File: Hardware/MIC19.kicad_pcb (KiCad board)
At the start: 2 copper layers, 160 x 70 mm, 101 parts, among them J101 SW_BOAT_ON, J102 ENGINE_VEL, J103 SW_PUMP1_ON, J104 SW_ENGINE_ON, J105 ENGINE_ACEL, J106 SW_PUMP2_ON, J107 SW_MPPT_ON, J108 MPPT_POT, J109 SW_PUMP3_ON, J110 SW_DMS, J111 SW_EMERGENCIA, J401 USART, J402 BUZZER ON/OFF, J601 RJ45, J602 RJ45, Q101 BCV27, U201 MCP2551-I/SN, U202 MCP2515-xSO, U401 ATMEGA328P-PU, U501 LM7805, Y201 16MHz, Y401 16MHz

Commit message: Modelo final
Terminado os conectores e a topologia
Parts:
- removed J402: BUZZER ON/OFF, Connector_PinHeader_2.54mm:PinHeader_1x02_P2.54mm_Vertical
- moved R115 9.53 mm to (75.5, 74.7), turned to 270 degrees
- moved R109 9.30 mm to (94.5, 74.7), turned to 270 degrees
- moved C103 9.01 mm to (103.5, 74.7), turned to 270 degrees
- moved R103 7.81 mm to (113.5, 74.7), turned to 270 degrees
- moved TP203 7.46 mm to (162.7, 129.4)
- moved R102 7.42 mm to (170.3, 74.7), turned to 270 degrees
- moved C108 6.78 mm to (122.5, 74.7), turned to 270 degrees
- moved C109 6.47 mm to (65.5, 74.7), turned to 270 degrees
- moved C106 6.30 mm to (84.5, 74.7), turned to 270 degrees
- moved R108 6.11 mm to (151.5, 74.7), turned to 270 degrees
- moved C105 5.57 mm to (141.5, 74.7), turned to 270 degrees
- moved R114 5.53 mm to (132.5, 74.7), turned to 270 degrees
- moved C102 5.38 mm to (160.3, 74.7), turned to 270 degrees
- moved R112 3.82 mm to (89.5, 74.7), turned to 90 degrees
- moved R105 2.19 mm to (165.3, 74.7), turned to 90 degrees
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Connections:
- D403 pad 1: Net-(D403-Pad1) -> Net-(BZ1-Pad1)
- Q101 pad 3: Net-(D403-Pad1) -> Net-(BZ1-Pad1)
- RV401 pad 1: Net-(D403-Pad1) -> Net-(BZ1-Pad1)
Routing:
- net +5V: track 143.4 -> 576.4 mm, vias 4 -> 26
- net /Conectores/ENGINE_VEL: track 0.00 -> 80.5 mm
- net /Conectores/ENGINE_ACEL: track 0.00 -> 63.4 mm
- net Net-(D403-Pad1): track 54.6 -> 0.00 mm
- net Net-(BZ1-Pad1): track 10.1 -> 64.6 mm
- net /Conectores/MPPT_POT: track 0.00 -> 47.0 mm
- net GND: track 90.7 -> 136.9 mm, vias 11 -> 17
- net /Conectores/SW_PUMP3_ON: track 0.00 -> 44.2 mm
- net /CANBUS/CS: track 21.9 -> 56.5 mm
- net /MISO: track 32.8 -> 66.0 mm
- net /MOSI: track 27.9 -> 60.2 mm
- net /Conectores/SW_PUMP1_ON: track 0.00 -> 32.2 mm
- net /Conectores/SW_PUMP2_ON: track 0.00 -> 31.5 mm
- net /SCK: track 30.8 -> 51.3 mm
- net /CANBUS/INT: track 16.8 -> 36.8 mm
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- added copper zone on B.Cu, net GND

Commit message: Buzzer estava invertido, alimentações melhoradas. A alimentação do atmega foi isolada em relação aos switches.
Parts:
- moved R406 13.0 mm to (59.8, 102.5)
- moved D403 8.16 mm to (59.8, 107.0), turned to 90 degrees
- moved C407 7.00 mm to (68.4, 108.1)
- moved Q101 7.00 mm to (63.9, 108.1)
- moved R404 7.00 mm to (73.4, 108.1)
- moved R405 7.00 mm to (70.9, 108.1)
- moved RV401 6.73 mm to (63.0, 99.0)
- moved D402 6.30 mm to (69.2, 99.8), turned to 270 degrees
- moved BZ1 6.25 mm to (72.5, 96.3)
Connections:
- D402 pad 1: Net-(BZ1-Pad2) -> Net-(BZ1-Pad1)
- D402 pad 2: Net-(BZ1-Pad1) -> Net-(BZ1-Pad2)
- D403 pad 1: Net-(BZ1-Pad1) -> Net-(BZ1-Pad2)
- Q101 pad 3: Net-(BZ1-Pad1) -> Net-(BZ1-Pad2)
- RV401 pad 1: Net-(BZ1-Pad1) -> +5V
- RV401 pad 2: Net-(BZ1-Pad2) -> Net-(BZ1-Pad1)
- RV401 pad 3: +5V -> Net-(BZ1-Pad2)
- U201 pad 5: Net-(U201-Pad5) -> (no net)
- U202 pad 10: Net-(U202-Pad10) -> (no net)
- U202 pad 11: Net-(U202-Pad11) -> (no net)
- U202 pad 3: Net-(U202-Pad3) -> (no net)
- U202 pad 4: Net-(U202-Pad4) -> (no net)
- U202 pad 5: Net-(U202-Pad5) -> (no net)
- U202 pad 6: Net-(U202-Pad6) -> (no net)
- U401 pad 16: Net-(U401-Pad16) -> (no net)
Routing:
- net Net-(BZ1-Pad1): track 64.6 -> 12.8 mm
- net +5V: track 576.4 -> 561.0 mm, vias 26 -> 24
- net /MCU/BUZZER: track 47.8 -> 40.7 mm
- net GND: track 136.9 -> 129.9 mm, vias 17 -> 15
- net Net-(BZ1-Pad2): track 16.5 -> 17.7 mm
- net /Conectores/MPPT_POT: track 47.0 -> 47.6 mm
- net /CANBUS CONN/CAN_H: track 63.3 -> 62.8 mm

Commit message: Roteamento de alimentação alterado e placa compactada.
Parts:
- moved C205 20.6 mm to (153.5, 119.2), turned to 90 degrees
- moved C204 13.7 mm to (135.7, 124.0)
- moved R203 13.7 mm to (147.3, 107.5)
- moved TP201 13.7 mm to (141.0, 103.6)
- moved TP202 13.7 mm to (144.2, 103.6)
- moved TP205 13.7 mm to (147.3, 103.6)
- moved TP206 13.7 mm to (137.8, 103.6)
- moved U202 13.7 mm to (142.0, 115.8)
- moved Y201 13.7 mm to (142.0, 126.6)
- moved C203 13.7 mm to (139.5, 126.2)
- moved D501 13.6 mm to (170.2, 88.8)
- moved TP204 13.5 mm to (150.8, 122.0)
- moved F501 13.3 mm to (167.2, 90.0)
- moved C501 12.4 mm to (163.8, 90.8)
- moved TP203 12.0 mm to (150.8, 128.5)
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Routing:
- net +5V: track 561.0 -> 630.6 mm, vias 24 -> 26
- net GND: track 129.9 -> 177.4 mm, vias 15 -> 12
- net /CANBUS/CS: track 56.5 -> 39.0 mm
- net /MISO: track 66.0 -> 49.2 mm
- net /MOSI: track 60.2 -> 44.9 mm
- net /CANBUS/INT: track 36.8 -> 25.8 mm
- net /CANBUS/TXCAN: track 14.1 -> 23.9 mm
- net /SCK: track 51.3 -> 42.0 mm
- net /POWER SUPPLY/+18V_IN: track 57.5 -> 65.1 mm
- net /CANBUS/RXCAN: track 16.7 -> 23.8 mm
- net /CANBUS CONN/CAN_H: track 62.8 -> 58.4 mm
- net Net-(R202-Pad1): track 6.64 -> 2.83 mm
- net Net-(C501-Pad1): track 19.5 -> 15.8 mm
- net Net-(J401-Pad2): track 6.59 -> 3.46 mm
- net Net-(J401-Pad3): track 6.59 -> 3.46 mm
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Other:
- board size 160 x 70 mm -> 160 x 70.2 mm

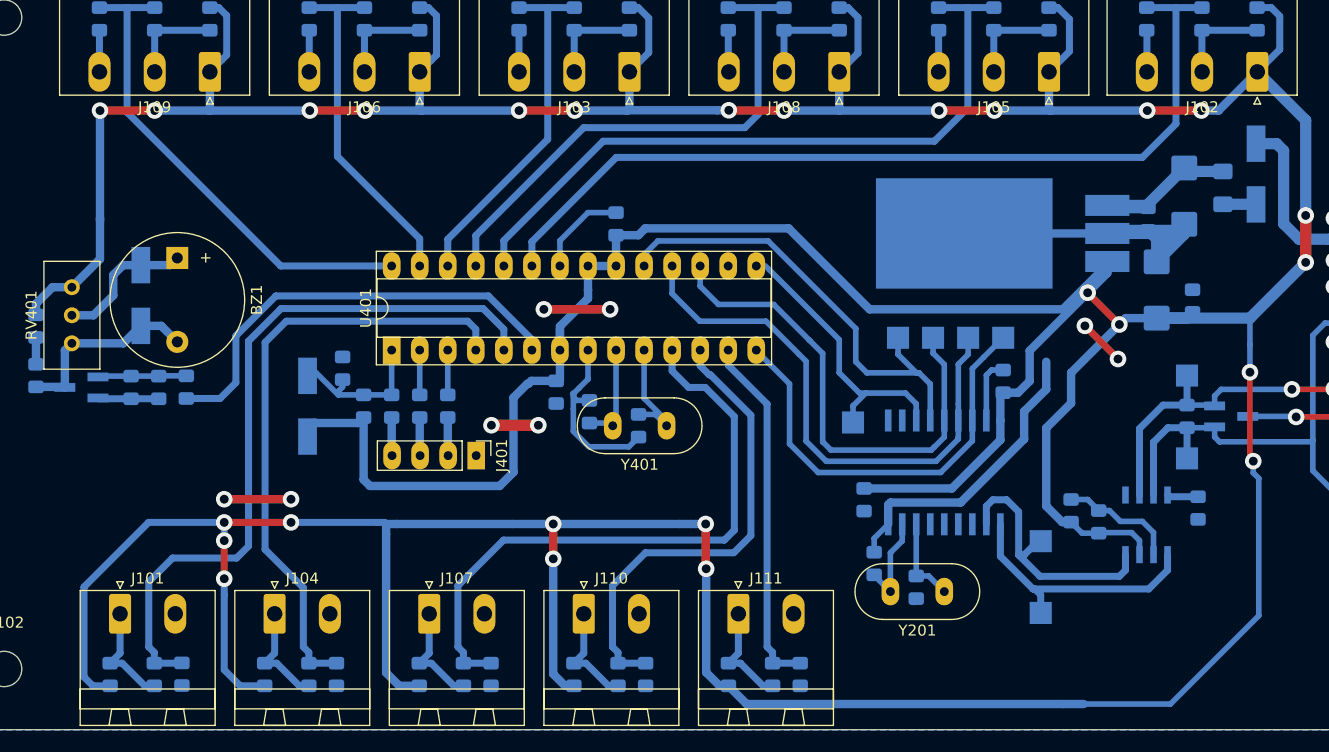
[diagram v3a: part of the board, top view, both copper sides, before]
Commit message: Final
Terminado detalhes que eram necessário para finalizar a placa, como trilhas de Vcc e Gnd remodeladas para melhor fluxo da corrente
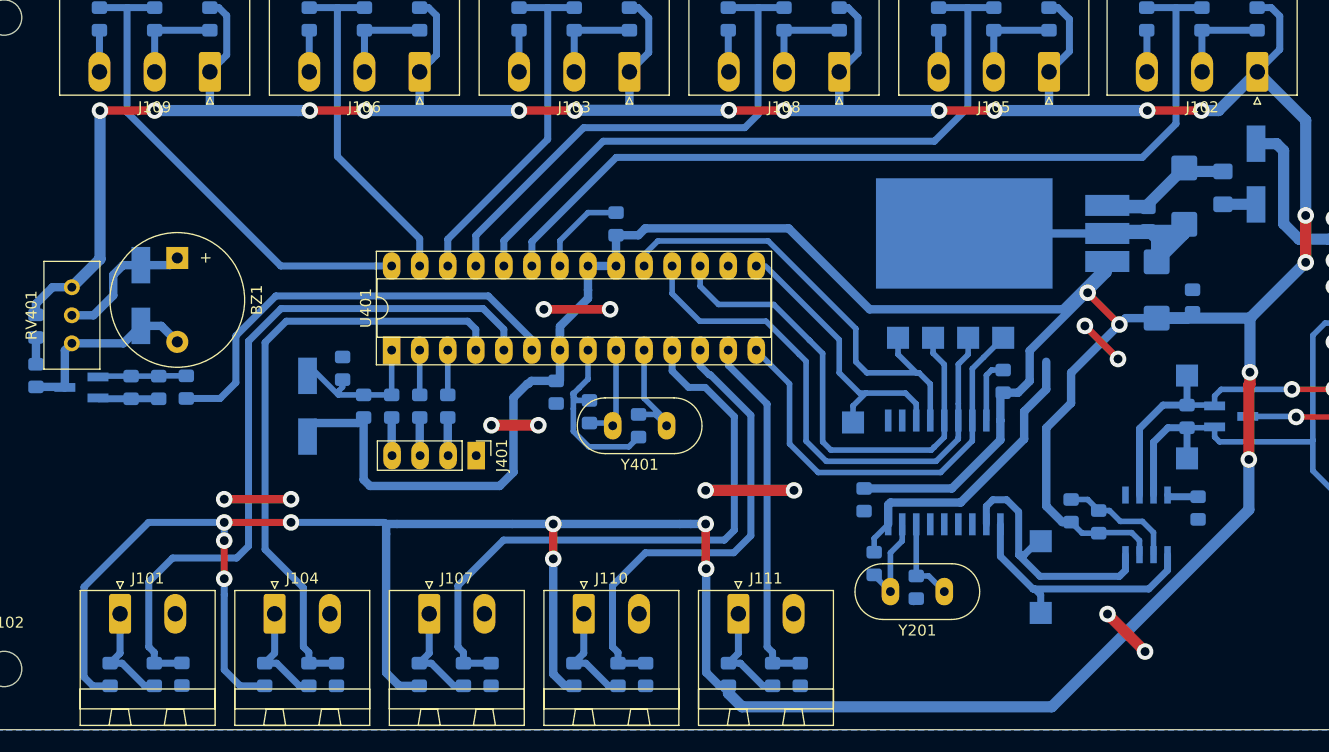
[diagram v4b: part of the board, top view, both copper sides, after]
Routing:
- net GND: track 177.4 -> 190.2 mm, vias 12 -> 16
- net +5V: track 630.6 -> 623.3 mm
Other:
- net class Default: clearance 0.508 -> 0.3
- net class power: clearance 0.762 -> 0.3
- rule trace_clearance: 0.508 -> 0.3

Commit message: Conferido e Finalizado
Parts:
- removed C405: 100nF, Capacitor_SMD:C_0805_2012Metric_Pad1.15x1.40mm_HandSolder
- added BZ1: Buzzer, Buzzer_Beeper:Buzzer_12x9.5RM7.6, F.Cu at (221.3, 158.4)
- added BZ1: Buzzer, Buzzer_Beeper:Buzzer_12x9.5RM7.6, F.Cu at (56.5, 136.3)
- added C101: 100n, Capacitor_SMD:C_0805_2012Metric_Pad1.15x1.40mm_HandSolder, B.Cu at (259.1, 158.0)
- added C101: 100n, Capacitor_SMD:C_0805_2012Metric_Pad1.15x1.40mm_HandSolder, B.Cu at (57.0, 174.1)
- added C102: 100n, Capacitor_SMD:C_0805_2012Metric_Pad1.15x1.40mm_HandSolder, B.Cu at (199.7, 70.7)
- added C102: 100n, Capacitor_SMD:C_0805_2012Metric_Pad1.15x1.40mm_HandSolder, B.Cu at (144.3, 114.7)
- added C103: 100n, Capacitor_SMD:C_0805_2012Metric_Pad1.15x1.40mm_HandSolder, B.Cu at (199.7, 127.5)
- added C103: 100n, Capacitor_SMD:C_0805_2012Metric_Pad1.15x1.40mm_HandSolder, B.Cu at (87.5, 114.7)
- added C104: 100n, Capacitor_SMD:C_0805_2012Metric_Pad1.15x1.40mm_HandSolder, B.Cu at (259.1, 144.0)
- added C104: 100n, Capacitor_SMD:C_0805_2012Metric_Pad1.15x1.40mm_HandSolder, B.Cu at (71.0, 174.1)
- added C105: 100n, Capacitor_SMD:C_0805_2012Metric_Pad1.15x1.40mm_HandSolder, B.Cu at (199.7, 89.5)
- added C105: 100n, Capacitor_SMD:C_0805_2012Metric_Pad1.15x1.40mm_HandSolder, B.Cu at (125.5, 114.7)
- added C106: 100n, Capacitor_SMD:C_0805_2012Metric_Pad1.15x1.40mm_HandSolder, B.Cu at (199.7, 146.5)
- added C106: 100n, Capacitor_SMD:C_0805_2012Metric_Pad1.15x1.40mm_HandSolder, B.Cu at (68.5, 114.7)
- added C107: 100n, Capacitor_SMD:C_0805_2012Metric_Pad1.15x1.40mm_HandSolder, B.Cu at (259.1, 130.0)
- added C107: 100n, Capacitor_SMD:C_0805_2012Metric_Pad1.15x1.40mm_HandSolder, B.Cu at (85.0, 174.1)
- added C108: 100n, Capacitor_SMD:C_0805_2012Metric_Pad1.15x1.40mm_HandSolder, B.Cu at (199.7, 108.5)
- added C108: 100n, Capacitor_SMD:C_0805_2012Metric_Pad1.15x1.40mm_HandSolder, B.Cu at (106.5, 114.7)
- added C109: 100n, Capacitor_SMD:C_0805_2012Metric_Pad1.15x1.40mm_HandSolder, B.Cu at (199.7, 165.5)
- added C109: 100n, Capacitor_SMD:C_0805_2012Metric_Pad1.15x1.40mm_HandSolder, B.Cu at (49.5, 114.7)
- added C110: 100n, Capacitor_SMD:C_0805_2012Metric_Pad1.15x1.40mm_HandSolder, B.Cu at (259.1, 116.0)
- added C110: 100n, Capacitor_SMD:C_0805_2012Metric_Pad1.15x1.40mm_HandSolder, B.Cu at (99.0, 174.1)
- added C111: 100n, Capacitor_SMD:C_0805_2012Metric_Pad1.15x1.40mm_HandSolder, B.Cu at (258.1, 96.8)
- added C111: 100n, Capacitor_SMD:C_0805_2012Metric_Pad1.15x1.40mm_HandSolder, B.Cu at (118.2, 173.1)
- added C201: 100nF, Capacitor_SMD:C_0805_2012Metric_Pad1.15x1.40mm_HandSolder, B.Cu at (243.2, 96.2)
- added C201: 100nF, Capacitor_SMD:C_0805_2012Metric_Pad1.15x1.40mm_HandSolder, B.Cu at (118.8, 158.2)
- added C202: 100nF, Capacitor_SMD:C_0805_2012Metric_Pad1.15x1.40mm_HandSolder, B.Cu at (245.2, 75.0)
- added C202: 100nF, Capacitor_SMD:C_0805_2012Metric_Pad1.15x1.40mm_HandSolder, B.Cu at (140.0, 160.2)
- added C203: 22pF, Capacitor_SMD:C_0805_2012Metric_Pad1.15x1.40mm_HandSolder, B.Cu at (251.2, 91.5)
- added C203: 22pF, Capacitor_SMD:C_0805_2012Metric_Pad1.15x1.40mm_HandSolder, B.Cu at (123.5, 166.2)
- added C204: 22pF, Capacitor_SMD:C_0805_2012Metric_Pad1.15x1.40mm_HandSolder, B.Cu at (249.0, 95.3)
- added C204: 22pF, Capacitor_SMD:C_0805_2012Metric_Pad1.15x1.40mm_HandSolder, B.Cu at (119.7, 164.0)
- added C205: 100nF, Capacitor_SMD:C_0805_2012Metric_Pad1.15x1.40mm_HandSolder, B.Cu at (244.2, 77.5)
- added C205: 100nF, Capacitor_SMD:C_0805_2012Metric_Pad1.15x1.40mm_HandSolder, B.Cu at (137.5, 159.2)
- added C401: 100nF, Capacitor_SMD:C_0805_2012Metric_Pad1.15x1.40mm_HandSolder, B.Cu at (218.3, 118.7)
- added C401: 100nF, Capacitor_SMD:C_0805_2012Metric_Pad1.15x1.40mm_HandSolder, B.Cu at (96.3, 133.3)
- added C402: 100nF, Capacitor_SMD:C_0805_2012Metric_Pad1.15x1.40mm_HandSolder, B.Cu at (233.5, 124.1)
- added C402: 100nF, Capacitor_SMD:C_0805_2012Metric_Pad1.15x1.40mm_HandSolder, B.Cu at (90.9, 148.5)
- added C403: 22pF, Capacitor_SMD:C_0805_2012Metric_Pad1.15x1.40mm_HandSolder, B.Cu at (236.5, 116.7)
- added C403: 22pF, Capacitor_SMD:C_0805_2012Metric_Pad1.15x1.40mm_HandSolder, B.Cu at (98.3, 151.5)
- added C404: 22pF, Capacitor_SMD:C_0805_2012Metric_Pad1.15x1.40mm_HandSolder, B.Cu at (235.3, 121.1)
- added C404: 22pF, Capacitor_SMD:C_0805_2012Metric_Pad1.15x1.40mm_HandSolder, B.Cu at (93.9, 150.3)
- added C406: 10nF, Capacitor_SMD:C_0805_2012Metric_Pad1.15x1.40mm_HandSolder, B.Cu at (231.3, 143.5)
- added C406: 10nF, Capacitor_SMD:C_0805_2012Metric_Pad1.15x1.40mm_HandSolder, B.Cu at (71.5, 146.3)
- added C407: 100nF, Capacitor_SMD:C_0805_2012Metric_Pad1.15x1.40mm_HandSolder, B.Cu at (233.1, 162.6)
- added C407: 100nF, Capacitor_SMD:C_0805_2012Metric_Pad1.15x1.40mm_HandSolder, B.Cu at (52.4, 148.1)
- added C501: 1uF, Capacitor_Tantalum_SMD:CP_EIA-6032-20_AVX-F_Pad2.25x2.35mm_HandSolder, B.Cu at (215.8, 67.2)
- added C501: 1uF, Capacitor_Tantalum_SMD:CP_EIA-6032-20_AVX-F_Pad2.25x2.35mm_HandSolder, B.Cu at (147.8, 130.8)
- added C502: 100nF, Capacitor_SMD:C_0805_2012Metric_Pad1.15x1.40mm_HandSolder, B.Cu at (217.8, 70.5)
- added C502: 100nF, Capacitor_SMD:C_0805_2012Metric_Pad1.15x1.40mm_HandSolder, B.Cu at (144.5, 132.8)
- added C503: 100nF, Capacitor_SMD:C_0805_2012Metric_Pad1.15x1.40mm_HandSolder, B.Cu at (225.2, 66.5)
- added C503: 100nF, Capacitor_SMD:C_0805_2012Metric_Pad1.15x1.40mm_HandSolder, B.Cu at (148.5, 140.2)
- added C504: 1uF, Capacitor_Tantalum_SMD:CP_EIA-6032-20_AVX-F_Pad2.25x2.35mm_HandSolder, B.Cu at (224.2, 69.8)
- added C504: 1uF, Capacitor_Tantalum_SMD:CP_EIA-6032-20_AVX-F_Pad2.25x2.35mm_HandSolder, B.Cu at (145.2, 139.2)
- added D201: pesd1can, Package_TO_SOT_SMD:SOT-23_Handsoldering, B.Cu at (235.7, 63.0)
- added D201: pesd1can, Package_TO_SOT_SMD:SOT-23_Handsoldering, B.Cu at (152.0, 150.7)
- added D401: LL4148, Diode_SMD:D_MiniMELF_Handsoldering, B.Cu at (234.8, 146.7)
- added D401: LL4148, Diode_SMD:D_MiniMELF_Handsoldering, B.Cu at (68.3, 149.8)
- added D402: BYD77, Diode_SMD:D_MiniMELF_Handsoldering, B.Cu at (224.8, 161.8)
- added D402: BYD77, Diode_SMD:D_MiniMELF_Handsoldering, B.Cu at (53.2, 139.8)
- added D403: LED_RED, LED_SMD:LED_0805_2012Metric_Pad1.15x1.40mm_HandSolder, B.Cu at (232.0, 171.2)
- added D403: LED_RED, LED_SMD:LED_0805_2012Metric_Pad1.15x1.40mm_HandSolder, B.Cu at (43.8, 147.0)
- added D501: LL4148, Diode_SMD:D_MiniMELF_Handsoldering, B.Cu at (213.8, 60.8)
- added D501: LL4148, Diode_SMD:D_MiniMELF_Handsoldering, B.Cu at (154.2, 128.8)
- added F501: 500mA, Fuse:Fuse_1206_3216Metric_Pad1.42x1.75mm_HandSolder, B.Cu at (215.0, 63.8)
- added F501: 500mA, Fuse:Fuse_1206_3216Metric_Pad1.42x1.75mm_HandSolder, B.Cu at (151.2, 130.0)
- added H101: MountingHole, MountingHole:MountingHole_3.2mm_M3, F.Cu at (199.6, 174.1)
- added H101: MountingHole, MountingHole:MountingHole_3.2mm_M3, F.Cu at (40.9, 114.6)
- added H102: MountingHole, MountingHole:MountingHole_3.2mm_M3, F.Cu at (258.6, 174.1)
- added H102: MountingHole, MountingHole:MountingHole_3.2mm_M3, F.Cu at (40.9, 173.6)
- added H103: MountingHole, MountingHole:MountingHole_3.2mm_M3, F.Cu at (199.3, 35.1)
- added H103: MountingHole, MountingHole:MountingHole_3.2mm_M3, F.Cu at (179.9, 114.3)
- added H104: MountingHole, MountingHole:MountingHole_3.2mm_M3, F.Cu at (258.3, 34.6)
- added H104: MountingHole, MountingHole:MountingHole_3.2mm_M3, F.Cu at (180.4, 173.3)
- added J101: SW_BOAT_ON, Connector_Phoenix_MSTB:PhoenixContact_MSTBA_2,5_2-G_1x02_P5.00mm_Horizontal, F.Cu at (253.6, 163.6)
- added J101: SW_BOAT_ON, Connector_Phoenix_MSTB:PhoenixContact_MSTBA_2,5_2-G_1x02_P5.00mm_Horizontal, F.Cu at (51.4, 168.6)
- added J102: ENGINE_VEL, Connector_Phoenix_MSTB:PhoenixContact_MSTBA_2,5_3-G_1x03_P5.00mm_Horizontal, F.Cu at (204.5, 60.6)
- added J102: ENGINE_VEL, Connector_Phoenix_MSTB:PhoenixContact_MSTBA_2,5_3-G_1x03_P5.00mm_Horizontal, F.Cu at (154.4, 119.5)
- added J103: SW_PUMP1_ON, Connector_Phoenix_MSTB:PhoenixContact_MSTBA_2,5_3-G_1x03_P5.00mm_Horizontal, F.Cu at (204.5, 117.5)
- added J103: SW_PUMP1_ON, Connector_Phoenix_MSTB:PhoenixContact_MSTBA_2,5_3-G_1x03_P5.00mm_Horizontal, F.Cu at (97.5, 119.5)
- added J104: SW_ENGINE_ON, Connector_Phoenix_MSTB:PhoenixContact_MSTBA_2,5_2-G_1x02_P5.00mm_Horizontal, F.Cu at (253.6, 149.6)
- added J104: SW_ENGINE_ON, Connector_Phoenix_MSTB:PhoenixContact_MSTBA_2,5_2-G_1x02_P5.00mm_Horizontal, F.Cu at (65.4, 168.6)
- added J105: ENGINE_ACEL, Connector_Phoenix_MSTB:PhoenixContact_MSTBA_2,5_3-G_1x03_P5.00mm_Horizontal, F.Cu at (204.5, 79.5)
- added J105: ENGINE_ACEL, Connector_Phoenix_MSTB:PhoenixContact_MSTBA_2,5_3-G_1x03_P5.00mm_Horizontal, F.Cu at (135.5, 119.5)
- added J106: SW_PUMP2_ON, Connector_Phoenix_MSTB:PhoenixContact_MSTBA_2,5_3-G_1x03_P5.00mm_Horizontal, F.Cu at (204.5, 136.5)
- added J106: SW_PUMP2_ON, Connector_Phoenix_MSTB:PhoenixContact_MSTBA_2,5_3-G_1x03_P5.00mm_Horizontal, F.Cu at (78.5, 119.5)
- added J107: SW_MPPT_ON, Connector_Phoenix_MSTB:PhoenixContact_MSTBA_2,5_2-G_1x02_P5.00mm_Horizontal, F.Cu at (253.6, 135.6)
- added J107: SW_MPPT_ON, Connector_Phoenix_MSTB:PhoenixContact_MSTBA_2,5_2-G_1x02_P5.00mm_Horizontal, F.Cu at (79.4, 168.6)
- added J108: MPPT_POT, Connector_Phoenix_MSTB:PhoenixContact_MSTBA_2,5_3-G_1x03_P5.00mm_Horizontal, F.Cu at (204.5, 98.5)
- added J108: MPPT_POT, Connector_Phoenix_MSTB:PhoenixContact_MSTBA_2,5_3-G_1x03_P5.00mm_Horizontal, F.Cu at (116.5, 119.5)
- added J109: SW_PUMP3_ON, Connector_Phoenix_MSTB:PhoenixContact_MSTBA_2,5_3-G_1x03_P5.00mm_Horizontal, F.Cu at (204.5, 155.5)
- added J109: SW_PUMP3_ON, Connector_Phoenix_MSTB:PhoenixContact_MSTBA_2,5_3-G_1x03_P5.00mm_Horizontal, F.Cu at (59.5, 119.5)
- added J110: SW_DMS, Connector_Phoenix_MSTB:PhoenixContact_MSTBA_2,5_2-G_1x02_P5.00mm_Horizontal, F.Cu at (253.6, 121.6)
- added J110: SW_DMS, Connector_Phoenix_MSTB:PhoenixContact_MSTBA_2,5_2-G_1x02_P5.00mm_Horizontal, F.Cu at (93.4, 168.6)
- added J111: SW_EMERGENCIA, Connector_Phoenix_MSTB:PhoenixContact_MSTBA_2,5_2-G_1x02_P5.00mm_Horizontal, F.Cu at (253.6, 107.6)
- added J111: SW_EMERGENCIA, Connector_Phoenix_MSTB:PhoenixContact_MSTBA_2,5_2-G_1x02_P5.00mm_Horizontal, F.Cu at (107.4, 168.6)
- added J401: USART, Connector_PinHeader_2.54mm:PinHeader_1x04_P2.54mm_Vertical, F.Cu at (239.2, 131.4)
- added J401: USART, Connector_PinHeader_2.54mm:PinHeader_1x04_P2.54mm_Vertical, F.Cu at (83.6, 154.2)
- added J601: RJ45, KicadZeniteSolarLibrary18:RJ45_YH59_01, F.Cu at (223.5, 46.7)
- added J601: RJ45, KicadZeniteSolarLibrary18:RJ45_YH59_01, F.Cu at (168.3, 138.5)
- added J602: RJ45, KicadZeniteSolarLibrary18:RJ45_YH59_01, F.Cu at (244.3, 46.7)
- added J602: RJ45, KicadZeniteSolarLibrary18:RJ45_YH59_01, F.Cu at (168.3, 159.3)
- added Q101: BCV27, Package_TO_SOT_SMD:SOT-23_Handsoldering, B.Cu at (233.1, 167.1)
- added Q101: BCV27, Package_TO_SOT_SMD:SOT-23_Handsoldering, B.Cu at (47.9, 148.1)
- added R101: 10k, Resistor_SMD:R_0805_2012Metric_Pad1.15x1.40mm_HandSolder, B.Cu at (259.1, 164.5)
- added R101: 10k, Resistor_SMD:R_0805_2012Metric_Pad1.15x1.40mm_HandSolder, B.Cu at (50.5, 174.1)
- added R102: 10k, Resistor_SMD:R_0805_2012Metric_Pad1.15x1.40mm_HandSolder, B.Cu at (199.7, 60.6)
- added R102: 10k, Resistor_SMD:R_0805_2012Metric_Pad1.15x1.40mm_HandSolder, B.Cu at (154.3, 114.7)
- added R103: 10k, Resistor_SMD:R_0805_2012Metric_Pad1.15x1.40mm_HandSolder, B.Cu at (199.7, 117.5)
- added R103: 10k, Resistor_SMD:R_0805_2012Metric_Pad1.15x1.40mm_HandSolder, B.Cu at (97.5, 114.7)
- added R104: 100R, Resistor_SMD:R_0805_2012Metric_Pad1.15x1.40mm_HandSolder, B.Cu at (259.1, 160.5)
- added R104: 100R, Resistor_SMD:R_0805_2012Metric_Pad1.15x1.40mm_HandSolder, B.Cu at (54.5, 174.1)
- added R105: 100R, Resistor_SMD:R_0805_2012Metric_Pad1.15x1.40mm_HandSolder, B.Cu at (199.7, 65.7)
- added R105: 100R, Resistor_SMD:R_0805_2012Metric_Pad1.15x1.40mm_HandSolder, B.Cu at (149.3, 114.7)
- added R106: 100R, Resistor_SMD:R_0805_2012Metric_Pad1.15x1.40mm_HandSolder, B.Cu at (199.7, 122.5)
- added R106: 100R, Resistor_SMD:R_0805_2012Metric_Pad1.15x1.40mm_HandSolder, B.Cu at (92.5, 114.7)
- added R107: 10k, Resistor_SMD:R_0805_2012Metric_Pad1.15x1.40mm_HandSolder, B.Cu at (259.1, 150.5)
- added R107: 10k, Resistor_SMD:R_0805_2012Metric_Pad1.15x1.40mm_HandSolder, B.Cu at (64.5, 174.1)
- added R108: 10k, Resistor_SMD:R_0805_2012Metric_Pad1.15x1.40mm_HandSolder, B.Cu at (199.7, 79.5)
- added R108: 10k, Resistor_SMD:R_0805_2012Metric_Pad1.15x1.40mm_HandSolder, B.Cu at (135.5, 114.7)
- added R109: 10k, Resistor_SMD:R_0805_2012Metric_Pad1.15x1.40mm_HandSolder, B.Cu at (199.7, 136.5)
- added R109: 10k, Resistor_SMD:R_0805_2012Metric_Pad1.15x1.40mm_HandSolder, B.Cu at (78.5, 114.7)
- added R110: 100R, Resistor_SMD:R_0805_2012Metric_Pad1.15x1.40mm_HandSolder, B.Cu at (259.1, 146.5)
- added R110: 100R, Resistor_SMD:R_0805_2012Metric_Pad1.15x1.40mm_HandSolder, B.Cu at (68.5, 174.1)
- added R111: 100R, Resistor_SMD:R_0805_2012Metric_Pad1.15x1.40mm_HandSolder, B.Cu at (199.7, 84.5)
- added R111: 100R, Resistor_SMD:R_0805_2012Metric_Pad1.15x1.40mm_HandSolder, B.Cu at (130.5, 114.7)
- added R112: 100R, Resistor_SMD:R_0805_2012Metric_Pad1.15x1.40mm_HandSolder, B.Cu at (199.7, 141.5)
- added R112: 100R, Resistor_SMD:R_0805_2012Metric_Pad1.15x1.40mm_HandSolder, B.Cu at (73.5, 114.7)
- added R113: 10k, Resistor_SMD:R_0805_2012Metric_Pad1.15x1.40mm_HandSolder, B.Cu at (259.1, 136.5)
- added R113: 10k, Resistor_SMD:R_0805_2012Metric_Pad1.15x1.40mm_HandSolder, B.Cu at (78.5, 174.1)
- added R114: 10k, Resistor_SMD:R_0805_2012Metric_Pad1.15x1.40mm_HandSolder, B.Cu at (199.7, 98.5)
- added R114: 10k, Resistor_SMD:R_0805_2012Metric_Pad1.15x1.40mm_HandSolder, B.Cu at (116.5, 114.7)
- added R115: 10k, Resistor_SMD:R_0805_2012Metric_Pad1.15x1.40mm_HandSolder, B.Cu at (199.7, 155.5)
- added R115: 10k, Resistor_SMD:R_0805_2012Metric_Pad1.15x1.40mm_HandSolder, B.Cu at (59.5, 114.7)
- added R116: 100R, Resistor_SMD:R_0805_2012Metric_Pad1.15x1.40mm_HandSolder, B.Cu at (259.1, 132.5)
- added R116: 100R, Resistor_SMD:R_0805_2012Metric_Pad1.15x1.40mm_HandSolder, B.Cu at (82.5, 174.1)
- added R117: 100R, Resistor_SMD:R_0805_2012Metric_Pad1.15x1.40mm_HandSolder, B.Cu at (199.7, 103.5)
- added R117: 100R, Resistor_SMD:R_0805_2012Metric_Pad1.15x1.40mm_HandSolder, B.Cu at (111.5, 114.7)
- added R118: 100R, Resistor_SMD:R_0805_2012Metric_Pad1.15x1.40mm_HandSolder, B.Cu at (199.7, 160.5)
- added R118: 100R, Resistor_SMD:R_0805_2012Metric_Pad1.15x1.40mm_HandSolder, B.Cu at (54.5, 114.7)
- added R119: 10k, Resistor_SMD:R_0805_2012Metric_Pad1.15x1.40mm_HandSolder, B.Cu at (259.1, 122.5)
- added R119: 10k, Resistor_SMD:R_0805_2012Metric_Pad1.15x1.40mm_HandSolder, B.Cu at (92.5, 174.1)
- added R120: 100R, Resistor_SMD:R_0805_2012Metric_Pad1.15x1.40mm_HandSolder, B.Cu at (259.1, 118.5)
- added R120: 100R, Resistor_SMD:R_0805_2012Metric_Pad1.15x1.40mm_HandSolder, B.Cu at (96.5, 174.1)
- added R121: 10k, Resistor_SMD:R_0805_2012Metric_Pad1.15x1.40mm_HandSolder, B.Cu at (259.1, 108.5)
- added R121: 10k, Resistor_SMD:R_0805_2012Metric_Pad1.15x1.40mm_HandSolder, B.Cu at (106.5, 174.1)
- added R122: 100R, Resistor_SMD:R_0805_2012Metric_Pad1.15x1.40mm_HandSolder, B.Cu at (258.1, 99.3)
- added R122: 100R, Resistor_SMD:R_0805_2012Metric_Pad1.15x1.40mm_HandSolder, B.Cu at (115.7, 173.1)
- added R201: 120, Resistor_SMD:R_0805_2012Metric_Pad1.15x1.40mm_HandSolder, B.Cu at (235.7, 67.0)
- added R201: 120, Resistor_SMD:R_0805_2012Metric_Pad1.15x1.40mm_HandSolder, B.Cu at (148.0, 150.7)
- added R202: 4k7, Resistor_SMD:R_0805_2012Metric_Pad1.15x1.40mm_HandSolder, B.Cu at (244.0, 66.0)
- added R202: 4k7, Resistor_SMD:R_0805_2012Metric_Pad1.15x1.40mm_HandSolder, B.Cu at (149.0, 159.0)
- added R203: 10k, Resistor_SMD:R_0805_2012Metric_Pad1.15x1.40mm_HandSolder, B.Cu at (232.5, 83.7)
- added R203: 10k, Resistor_SMD:R_0805_2012Metric_Pad1.15x1.40mm_HandSolder, B.Cu at (131.3, 147.5)
- added R401: 10k, Resistor_SMD:R_0805_2012Metric_Pad1.15x1.40mm_HandSolder, B.Cu at (236.5, 141.6)
- added R401: 10k, Resistor_SMD:R_0805_2012Metric_Pad1.15x1.40mm_HandSolder, B.Cu at (73.4, 151.5)
- added R402: 100R, Resistor_SMD:R_0805_2012Metric_Pad1.15x1.40mm_HandSolder, B.Cu at (234.8, 136.5)
- added R402: 100R, Resistor_SMD:R_0805_2012Metric_Pad1.15x1.40mm_HandSolder, B.Cu at (78.5, 149.8)
- added R403: 100R, Resistor_SMD:R_0805_2012Metric_Pad1.15x1.40mm_HandSolder, B.Cu at (234.8, 134.0)
- added R403: 100R, Resistor_SMD:R_0805_2012Metric_Pad1.15x1.40mm_HandSolder, B.Cu at (81.0, 149.8)
- added R404: 100R, Resistor_SMD:R_0805_2012Metric_Pad1.15x1.40mm_HandSolder, B.Cu at (233.1, 157.6)
- added R404: 100R, Resistor_SMD:R_0805_2012Metric_Pad1.15x1.40mm_HandSolder, B.Cu at (57.4, 148.1)
- added R405: 100R, Resistor_SMD:R_0805_2012Metric_Pad1.15x1.40mm_HandSolder, B.Cu at (233.1, 160.1)
- added R405: 100R, Resistor_SMD:R_0805_2012Metric_Pad1.15x1.40mm_HandSolder, B.Cu at (54.9, 148.1)
- added R406: 330, Resistor_SMD:R_0805_2012Metric_Pad1.15x1.40mm_HandSolder, B.Cu at (227.5, 171.2)
- added R406: 330, Resistor_SMD:R_0805_2012Metric_Pad1.15x1.40mm_HandSolder, B.Cu at (43.8, 142.5)
- added R407: 100R, Resistor_SMD:R_0805_2012Metric_Pad1.15x1.40mm_HandSolder, B.Cu at (234.8, 139.0)
- added R407: 100R, Resistor_SMD:R_0805_2012Metric_Pad1.15x1.40mm_HandSolder, B.Cu at (76.0, 149.8)
- added R407: 100R, Resistor_SMD:R_0805_2012Metric_Pad1.15x1.40mm_HandSolder, B.Cu at (76.0, 69.8)
- added RV401: 1K, Potentiometer_THT:Potentiometer_Bourns_3296W_Vertical, F.Cu at (224.0, 168.0)
- added RV401: 1K, Potentiometer_THT:Potentiometer_Bourns_3296W_Vertical, F.Cu at (47.0, 139.0)
- added TP201: SI, TestPoint:TestPoint_Pad_2.0x2.0mm, B.Cu at (228.6, 90.0)
- added TP201: SI, TestPoint:TestPoint_Pad_2.0x2.0mm, B.Cu at (125.0, 143.6)
- added TP202: SO, TestPoint:TestPoint_Pad_2.0x2.0mm, B.Cu at (228.6, 86.8)
- added TP202: SO, TestPoint:TestPoint_Pad_2.0x2.0mm, B.Cu at (128.2, 143.6)
- added TP203: TXCAN, TestPoint:TestPoint_Pad_2.0x2.0mm, B.Cu at (253.5, 80.2)
- added TP203: TXCAN, TestPoint:TestPoint_Pad_2.0x2.0mm, B.Cu at (134.8, 168.5)
- added TP204: RXCAN, TestPoint:TestPoint_Pad_2.0x2.0mm, B.Cu at (247.0, 80.2)
- added TP204: RXCAN, TestPoint:TestPoint_Pad_2.0x2.0mm, B.Cu at (134.8, 162.0)
- added TP205: SC, TestPoint:TestPoint_Pad_2.0x2.0mm, B.Cu at (228.6, 83.7)
- added TP205: SC, TestPoint:TestPoint_Pad_2.0x2.0mm, B.Cu at (131.3, 143.6)
- added TP206: SCK, TestPoint:TestPoint_Pad_2.0x2.0mm, B.Cu at (228.6, 93.2)
- added TP206: SCK, TestPoint:TestPoint_Pad_2.0x2.0mm, B.Cu at (121.8, 143.6)
- added TP207: CAN_H, TestPoint:TestPoint_Pad_2.0x2.0mm, B.Cu at (239.5, 67.0)
- added TP207: CAN_H, TestPoint:TestPoint_Pad_2.0x2.0mm, B.Cu at (148.0, 154.5)
- added TP208: CAN_L, TestPoint:TestPoint_Pad_2.0x2.0mm, B.Cu at (232.0, 67.0)
- added TP208: CAN_L, TestPoint:TestPoint_Pad_2.0x2.0mm, B.Cu at (148.0, 147.0)
- added TP209: INT, TestPoint:TestPoint_Pad_2.0x2.0mm, B.Cu at (236.2, 97.2)
- added TP209: INT, TestPoint:TestPoint_Pad_2.0x2.0mm, B.Cu at (117.8, 151.2)
- added U201: MCP2551-I/SN, Package_SO:SOIC-8_3.9x4.9mm_P1.27mm, B.Cu at (245.5, 70.7)
- added U201: MCP2551-I/SN, Package_SO:SOIC-8_3.9x4.9mm_P1.27mm, B.Cu at (144.3, 160.5)
- added U202: MCP2515-xSO, Package_SO:SOIC-18W_7.5x11.6mm_P1.27mm, B.Cu at (240.8, 89.0)
- added U202: MCP2515-xSO, Package_SO:SOIC-18W_7.5x11.6mm_P1.27mm, B.Cu at (126.0, 155.8)
- added U401: ATMEGA328P-PU, Package_DIP:DIP-28_W7.62mm_Socket, F.Cu at (229.7, 139.0)
- added U401: ATMEGA328P-PU, Package_DIP:DIP-28_W7.62mm_Socket, F.Cu at (76.0, 144.7)
- added U501: LM7805, KicadZeniteSolarLibrary18:TO-220-3_Horizontal_TabDown_SMD, B.Cu at (216.6, 75.5)
- added U501: LM7805, KicadZeniteSolarLibrary18:TO-220-3_Horizontal_TabDown_SMD, B.Cu at (139.5, 131.6)
- added Y201: 16MHz, Crystal:Crystal_HC49-U_Vertical, F.Cu at (251.6, 89.0)
- added Y201: 16MHz, Crystal:Crystal_HC49-U_Vertical, F.Cu at (126.0, 166.6)
- added Y401: 16MHz, Crystal:Crystal_HC49-U_Vertical, F.Cu at (236.5, 114.1)
- added Y401: 16MHz, Crystal:Crystal_HC49-U_Vertical, F.Cu at (100.9, 151.5)
- C406: value 100nF -> 10nF
- R402, R403: value 1k -> 100R
- moved C102 43.1 mm to (144.3, 34.7)
- moved C103 43.1 mm to (87.5, 34.7)
- moved C104 43.1 mm to (71.0, 94.1)
- moved C105 43.1 mm to (125.5, 34.7)
- moved C106 43.1 mm to (68.5, 34.7)
- moved C107 43.1 mm to (85.0, 94.1)
- moved C108 43.1 mm to (106.5, 34.7)
- moved C109 43.1 mm to (49.5, 34.7)
- moved C110 43.1 mm to (99.0, 94.1)
- moved C201 43.1 mm to (118.8, 78.2)
- moved C202 43.1 mm to (140.0, 80.2)
- moved C203 43.1 mm to (123.5, 86.2)
- moved C204 43.1 mm to (119.7, 84.0)
- moved C205 43.1 mm to (137.5, 79.2)
- moved C401 43.1 mm to (96.3, 53.3)
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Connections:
- J401 pad 4: Net-(C405-Pad2) -> /MCU/RESET
- U401 pad 1: /MCU/RESET -> Net-(R407-Pad1)
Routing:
- net (no net): track 0.00 -> 4250.7 mm, vias 0 -> 120
- net GND: track 190.2 -> 222.2 mm, vias 16 -> 30
- net +5V: track 623.3 -> 632.3 mm
- net Net-(J111-Pad1): track 9.70 -> 15.4 mm
- net /Conectores/SW_EMERGENCIA: track 32.5 -> 36.4 mm
- net Net-(R407-Pad1): track 0.00 -> 3.79 mm
- net Net-(C405-Pad2): track 3.46 -> 0.00 mm
- net /MCU/RESET: track 14.2 -> 13.4 mm
- added copper zone on B.Cu, net (none)
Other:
- board size 160 x 70.2 mm -> 228 x 149.8 mm
